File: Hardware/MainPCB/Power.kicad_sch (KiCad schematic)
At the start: 25 parts, among them J12 USB_B_Micro

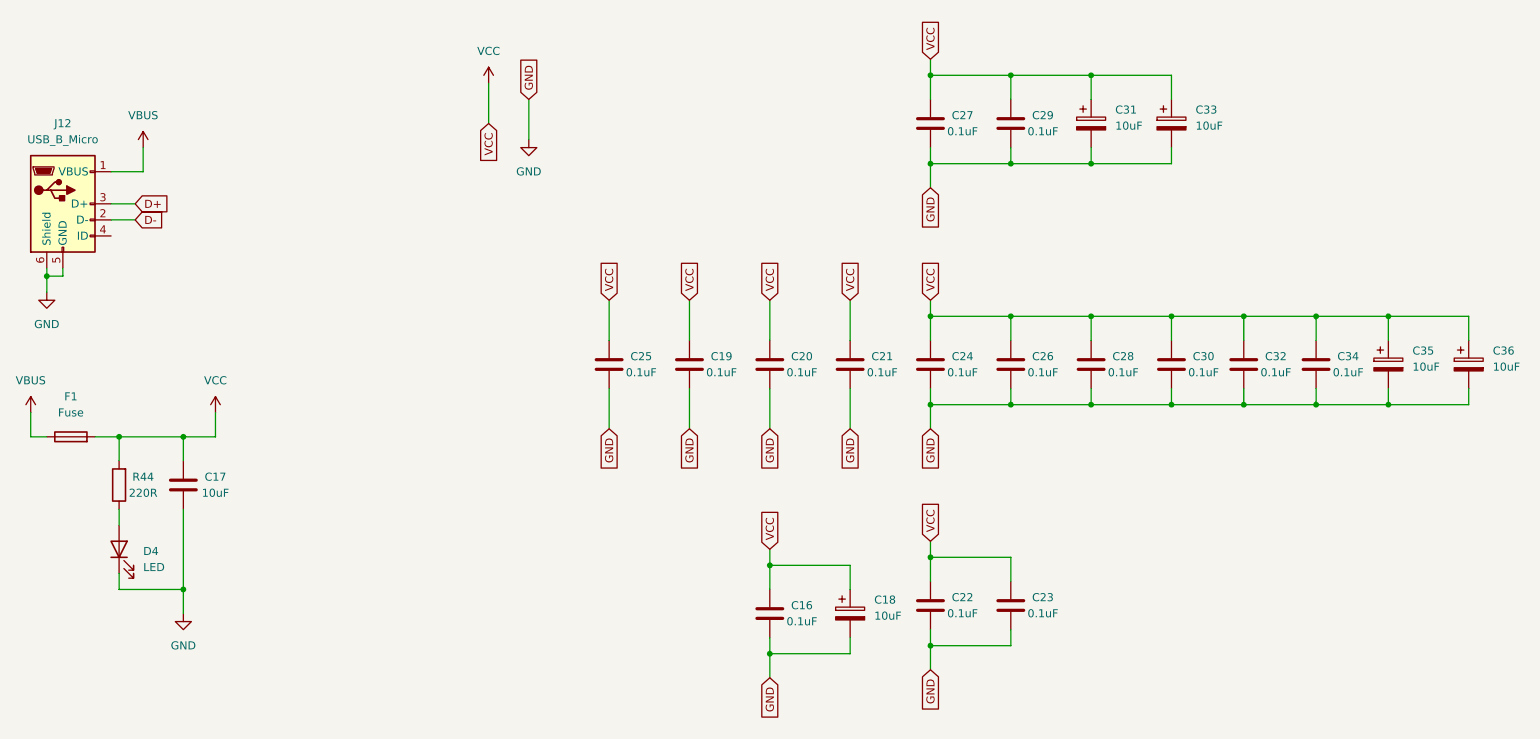
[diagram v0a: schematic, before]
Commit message: Fixed color bending issue; Added diagnostics
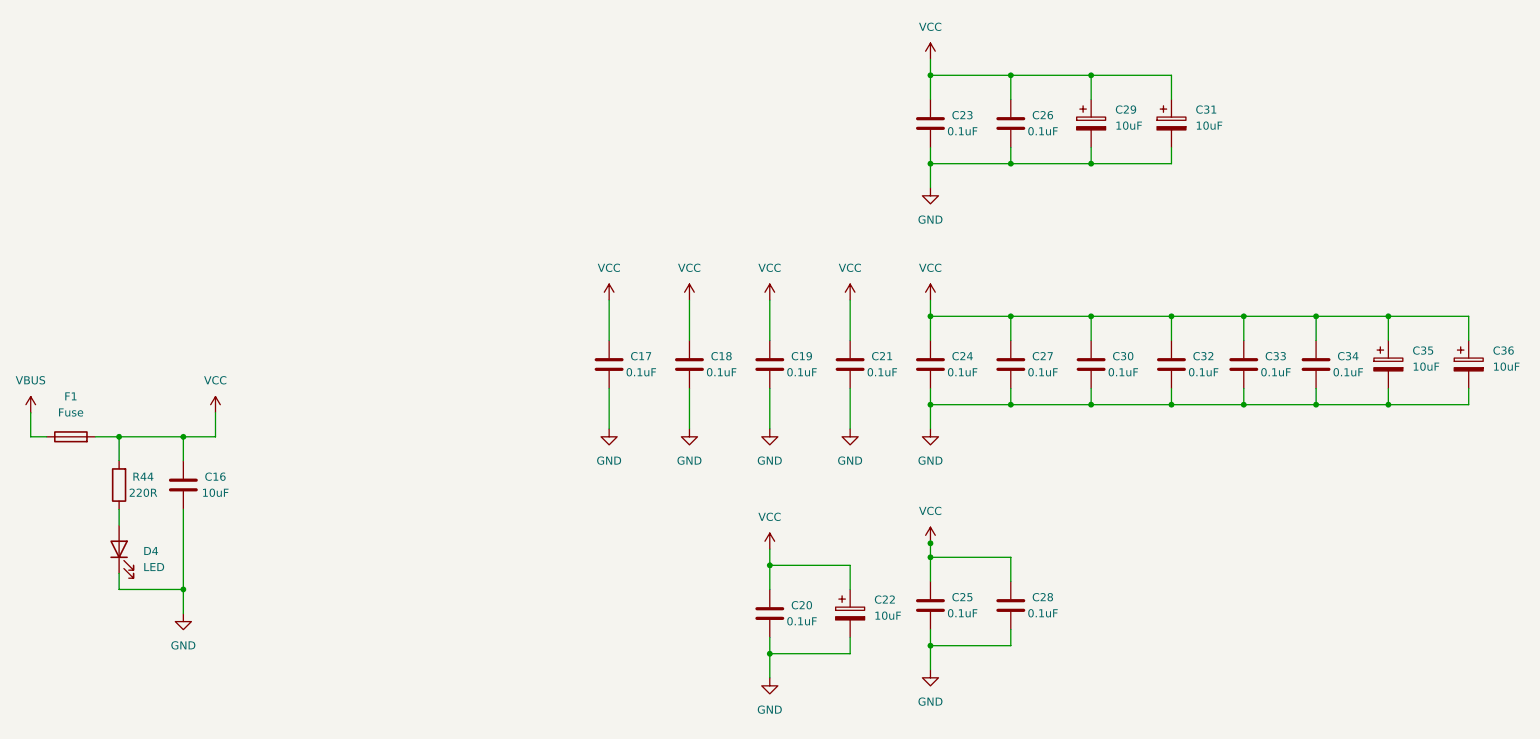
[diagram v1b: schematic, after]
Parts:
- removed J12: USB_B_Micro, Connector_USB:USB_Micro-B_Molex-105017-0001, symbol Connector:USB_B_Micro
- R44: footprint Resistor_SMD:R_0603_1608Metric -> RT5XP-EXP:R_0603; symbol Device:R -> RT5XP_EXP:R
- renumbered C17 to C16, C25 to C17, C19 to C18, C20 to C19, C16 to C20, C18 to C22, C27 to C23, C22 to C25, C29 to C26, C26 to C27, C23 to C28, C31 to C29, C28 to C30, C33 to C31, C30 to C32, C32 to C33
